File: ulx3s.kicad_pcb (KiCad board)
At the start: 4 copper layers, 60.1 x 34.8 mm, 87 parts, among them J3 hub75-abcd, J4 CONN_02X03, J5 hub75-abcd, J6 WIFI_OFF, U1 LFE5U-85F-6BG381C, U10 IS25LP128F-JBLE, U11 MPM54304GMN-0001, U2 IS42S16160J-6BL, U6 FT231XS, U9 ESP32-S3-WROOM-1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

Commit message: reassign j1 signals
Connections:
- J3 pad 1: unconnected-(J3-R1-Pad1) -> GP0
- J3 pad 10: unconnected-(J3-ROW1-Pad10) -> GN3
- J3 pad 11: unconnected-(J3-ROW2-Pad11) -> GP4
- J3 pad 12: unconnected-(J3-ROW3-Pad12) -> GN4
- J3 pad 13: unconnected-(J3-PXC-Pad13) -> GP5
- J3 pad 14: unconnected-(J3-RWL-Pad14) -> GN5
- J3 pad 15: unconnected-(J3-nOE-Pad15) -> GP6
- J3 pad 16: unconnected-(J3-GND-Pad16) -> GND
- J3 pad 2: unconnected-(J3-G1-Pad2) -> GN0
- J3 pad 3: unconnected-(J3-B1-Pad3) -> GP1
- J3 pad 4: unconnected-(J3-GND-Pad4) -> GND
- J3 pad 5: unconnected-(J3-R2-Pad5) -> GN1
- J3 pad 6: unconnected-(J3-G2-Pad6) -> GP2
- J3 pad 7: unconnected-(J3-B2-Pad7) -> GN2
- J3 pad 8: unconnected-(J3-GND-Pad8) -> GND
- J3 pad 9: unconnected-(J3-ROW0-Pad9) -> GP3
- J5 pad 1: unconnected-(J5-R1-Pad1) -> GP7
- J5 pad 10: unconnected-(J5-ROW1-Pad10) -> GN10
- J5 pad 11: unconnected-(J5-ROW2-Pad11) -> GP11
- J5 pad 12: unconnected-(J5-ROW3-Pad12) -> GN11
- J5 pad 13: unconnected-(J5-PXC-Pad13) -> GP12
- J5 pad 14: unconnected-(J5-RWL-Pad14) -> GN12
- J5 pad 15: unconnected-(J5-nOE-Pad15) -> GP13
- J5 pad 16: unconnected-(J5-GND-Pad16) -> GND
- J5 pad 2: unconnected-(J5-G1-Pad2) -> GN7
- J5 pad 3: unconnected-(J5-B1-Pad3) -> GP8
- J5 pad 4: unconnected-(J5-GND-Pad4) -> GND
- J5 pad 5: unconnected-(J5-R2-Pad5) -> GN8
- J5 pad 6: unconnected-(J5-G2-Pad6) -> GP9
- J5 pad 7: unconnected-(J5-B2-Pad7) -> GN9
- J5 pad 8: unconnected-(J5-GND-Pad8) -> GND
- J5 pad 9: unconnected-(J5-ROW0-Pad9) -> GP10
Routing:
- net unconnected-(J5-GND-Pad8): track 6.40 -> 0.00 mm
- net GND: track 305.4 -> 311.8 mm
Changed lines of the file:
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@@
 			)
 		)
-		(property "Datasheet" ""
+		(property "Datasheet" "https://www.espressif.com/sites/default/files/documentation/esp32-s3-wroom-1_wroom-1u_datasheet_en.pdf"
 			(at 0 0 90)
 			(layer "F.Fab")
@@
 			)
 		)
-		(property "Description" ""
+		(property "Description" "2.4 GHz WiFi (802.11 b/g/n) and Bluetooth ® 5 (LE) module Built around ESP32S3 series of SoCs, Xtensa ® dualcore 32bit LX7 microprocessor Flash up to 16 MB, PSRAM up to 8 MB 36 GPIOs, rich set of peripherals Onboard PCB antenna"
 			(at 0 0 90)
 			(layer "F.Fab")
@@
 			)
 		)
+		(property "Arrow" ""
+			(at 0 0 90)
+			(unlocked yes)
+			(layer "F.Fab")
+			(hide yes)
+			(effects
+				(font
+					(size 1 1)
+					(thickness 0.15)
+				)
+			)
+		)
+		(property "DatasheetLC" ""
+			(at 0 0 90)
+			(unlocked yes)
+			(layer "F.Fab")
+			(hide yes)
+			(effects
+				(font
+					(size 1 1)
+					(thickness 0.15)
+				)
+			)
+		)
+		(property "LCS_C2" ""
+			(at 0 0 90)
+			(unlocked yes)
+			(layer "F.Fab")
+			(hide yes)
+			(effects
+				(font
+					(size 1 1)
+					(thickness 0.15)
+				)
+			)
+		)
+		(property "MP_N4" ""
+			(at 0 0 90)
+			(unlocked yes)
+			(layer "F.Fab")
+			(hide yes)
+			(effects
+				(font
+					(size 1 1)
+					(thickness 0.15)
+				)
+			)
+		)
+		(property "MP_N5" ""
+			(at 0 0 90)
+			(unlocked yes)
+			(layer "F.Fab")
+			(hide yes)
+			(effects
+				(font
+					(size 1 1)
+					(thickness 0.15)
+				)
+			)
+		)
+		(property "Vertical" ""
+			(at 0 0 90)
+			(unlocked yes)
+			(layer "F.Fab")
+			(hide yes)
+			(effects
+				(font
+					(size 1 1)
+					(thickness 0.15)
+				)
+			)
+		)
+		(property "price100_Mouser" ""
+			(at 0 0 90)
+			(unlocked yes)
+			(layer "F.Fab")
+			(hide yes)
+			(effects
+				(font
+					(size 1 1)
+					(thickness 0.15)
+				)
+			)
+		)
+		(property "price1200_Chip1stop" ""
+			(at 0 0 90)
+			(unlocked yes)
+			(layer "F.Fab")
+			(hide yes)
+			(effects
+				(font
+					(size 1 1)
+					(thickness 0.15)
+				)
+			)
+		)
+		(property "price300_LCSC" ""
+			(at 0 0 90)
+			(unlocked yes)
+			(layer "F.Fab")
+			(hide yes)
+			(effects
+				(font
+					(size 1 1)
+					(thickness 0.15)
+				)
+			)
+		)
+		(property "price300_Vertical" ""
+			(at 0 0 90)
+			(unlocked yes)
+			(layer "F.Fab")
+			(hide yes)
+			(effects
+				(font
+					(size 1 1)
+					(thickness 0.15)
+				)
+			)
+		)
+		(property "price_Arrow" ""
+			(at 0 0 90)
+			(unlocked yes)
+			(layer "F.Fab")
+			(hide yes)
+			(effects
+				(font
+					(size 1 1)
+					(thickness 0.15)
+				)
+			)
+		)
+		(property "Digikey" "5407-ESP32-S3-WROOM-1-N16R8CT-ND"
+			(at 0 0 90)
+			(unlocked yes)
+			(layer "F.Fab")
+			(hide yes)
+			(effects
+				(font
+					(size 1 1)
+					(thickness 0.15)
+				)
+			)
+		)
+		(property "MPN" "356-ESP32S3WRM1N16R8"
+			(at 0 0 90)
+			(unlocked yes)
+			(layer "F.Fab")
+			(hide yes)
+			(effects
+				(font
+					(size 1 1)
+					(thickness 0.15)
+				)
+			)
+		)
 		(sheetname "/wifi/")
 		(sheetfile "wifi.kicad_sch")
+		(units
+			(unit
+				(name "A")
+				(pins "3" "8" "9" "32" "33" "34" "35" "28" "29" "30" "2" "41" "1" "40"
+					"37" "36" "14" "13" "27" "39" "38" "15" "4" "5" "6" "7" "12" "17" "18"
+					"19" "20" "21" "22" "10" "11" "23" "31" "26" "16" "24" "25"
+				)
+			)
+		)
 		(attr smd)
 		(duplicate_pad_numbers_are_jumpers no)
@@
 			(size 1.27 5.08)
 			(layers "B.Cu" "B.Paste")
-			(net "unconnected-(J3-R1-Pad1)")
+			(net "GP0")
 			(pinfunction "R1_1")
 			(pintype "input")
@@
 			(size 1.27 5.08)
 			(layers "B.Cu" "B.Paste")
-			(net "unconnected-(J3-G1-Pad2)")
+			(net "GN0")
 			(pinfunction "G1_2")
 			(pintype "input")
@@
 			(size 1.27 5.08)
 			(layers "B.Cu" "B.Paste")
-			(net "unconnected-(J3-B1-Pad3)")
+			(net "GP1")
 			(pinfunction "B1_3")
 			(pintype "input")
@@
 			(size 1.27 5.08)
 			(layers "B.Cu" "B.Paste")
-			(net "unconnected-(J3-GND-Pad4)")
+			(net "GND")
 			(pinfunction "GND_4")
 			(pintype "power_in")
@@
 			(size 1.27 5.08)
 			(layers "B.Cu" "B.Paste")
-			(net "unconnected-(J3-R2-Pad5)")
+			(net "GN1")
 			(pinfunction "R2_5")
 			(pintype "input")
@@
 			(size 1.27 5.08)
 			(layers "B.Cu" "B.Paste")
-			(net "unconnected-(J3-G2-Pad6)")
+			(net "GP2")
 			(pinfunction "G2_6")
 			(pintype "input")
@@
 			(size 1.27 5.08)
 			(layers "B.Cu" "B.Paste")
-			(net "unconnected-(J3-B2-Pad7)")
+			(net "GN2")
 			(pinfunction "B2_7")
 			(pintype "input")
@@
 			(size 1.27 5.08)
 			(layers "B.Cu" "B.Paste")
-			(net "unconnected-(J3-GND-Pad8)")
+			(net "GND")
 			(pinfunction "GND_8")
 			(pintype "power_in")
@@
 			(size 1.27 5.08)
 			(layers "B.Cu" "B.Paste")
-			(net "unconnected-(J3-ROW0-Pad9)")
+			(net "GP3")
 			(pinfunction "ROW0_9")
 			(pintype "input")
@@
 			(size 1.27 5.08)
 			(layers "B.Cu" "B.Paste")
-			(net "unconnected-(J3-ROW1-Pad10)")
+			(net "GN3")
 			(pinfunction "ROW1_10")
 			(pintype "input")
@@
 			(size 1.27 5.08)
 			(layers "B.Cu" "B.Paste")
-			(net "unconnected-(J3-ROW2-Pad11)")
+			(net "GP4")
 			(pinfunction "ROW2_11")
 			(pintype "input")
@@
 			(size 1.27 5.08)
 			(layers "B.Cu" "B.Paste")
-			(net "unconnected-(J3-ROW3-Pad12)")
+			(net "GN4")
 			(pinfunction "ROW3_12")
 			(pintype "input")
@@
 			(size 1.27 5.08)
 			(layers "B.Cu" "B.Paste")
-			(net "unconnected-(J3-PXC-Pad13)")
+			(net "GP5")
 			(pinfunction "PXC_13")
 			(pintype "input")
@@
 			(size 1.27 5.08)
 			(layers "B.Cu" "B.Paste")
-			(net "unconnected-(J3-RWL-Pad14)")
+			(net "GN5")
 			(pinfunction "RWL_14")
 			(pintype "input")
@@
 			(size 1.27 5.08)
 			(layers "B.Cu" "B.Paste")
-			(net "unconnected-(J3-nOE-Pad15)")
+			(net "GP6")
 			(pinfunction "nOE_15")
 			(pintype "input")
@@
 			(size 1.27 5.08)
 			(layers "B.Cu" "B.Paste")
-			(net "unconnected-(J3-GND-Pad16)")
+			(net "GND")
 			(pinfunction "GND_16")
 			(pintype "power_in")
@@
 			(size 1.27 5.08)
 			(layers "B.Cu" "B.Paste")
-			(net "unconnected-(J5-R1-Pad1)")
+			(net "GP7")
 			(pinfunction "R1_1")
 			(pintype "input")
@@
 			(size 1.27 5.08)
 			(layers "B.Cu" "B.Paste")
-			(net "unconnected-(J5-G1-Pad2)")
+			(net "GN7")
 			(pinfunction "G1_2")
 			(pintype "input")
@@
 			(size 1.27 5.08)
 			(layers "B.Cu" "B.Paste")
-			(net "unconnected-(J5-B1-Pad3)")
+			(net "GP8")
 			(pinfunction "B1_3")
 			(pintype "input")
@@
 			(size 1.27 5.08)
 			(layers "B.Cu" "B.Paste")
-			(net "unconnected-(J5-GND-Pad4)")
+			(net "GND")
 			(pinfunction "GND_4")
 			(pintype "power_in")
@@
 			(size 1.27 5.08)
 			(layers "B.Cu" "B.Paste")
-			(net "unconnected-(J5-R2-Pad5)")
+			(net "GN8")
 			(pinfunction "R2_5")
 			(pintype "input")
@@
 			(size 1.27 5.08)
 			(layers "B.Cu" "B.Paste")
-			(net "unconnected-(J5-G2-Pad6)")
+			(net "GP9")
 			(pinfunction "G2_6")
 			(pintype "input")
@@
 			(size 1.27 5.08)
 			(layers "B.Cu" "B.Paste")
-			(net "unconnected-(J5-B2-Pad7)")
+			(net "GN9")
 			(pinfunction "B2_7")
 			(pintype "input")
@@
 			(size 1.27 5.08)
 			(layers "B.Cu" "B.Paste")
-			(net "unconnected-(J5-GND-Pad8)")
+			(net "GND")
 			(pinfunction "GND_8")
 			(pintype "power_in")
@@
 			(size 1.27 5.08)
 			(layers "B.Cu" "B.Paste")
-			(net "unconnected-(J5-ROW0-Pad9)")
+			(net "GP10")
 			(pinfunction "ROW0_9")
 			(pintype "input")
@@
 			(size 1.27 5.08)
 			(layers "B.Cu" "B.Paste")
-			(net "unconnected-(J5-ROW1-Pad10)")
+			(net "GN10")
 			(pinfunction "ROW1_10")
 			(pintype "input")
@@
 			(size 1.27 5.08)
 			(layers "B.Cu" "B.Paste")
-			(net "unconnected-(J5-ROW2-Pad11)")
+			(net "GP11")
 			(pinfunction "ROW2_11")
 			(pintype "input")
@@
 			(size 1.27 5.08)
 			(layers "B.Cu" "B.Paste")
-			(net "unconnected-(J5-ROW3-Pad12)")
+			(net "GN11")
 			(pinfunction "ROW3_12")
 			(pintype "input")
@@
 			(size 1.27 5.08)
 			(layers "B.Cu" "B.Paste")
-			(net "unconnected-(J5-PXC-Pad13)")
+			(net "GP12")
 			(pinfunction "PXC_13")
 			(pintype "input")
@@
 			(size 1.27 5.08)
 			(layers "B.Cu" "B.Paste")
-			(net "unconnected-(J5-RWL-Pad14)")
+			(net "GN12")
 			(pinfunction "RWL_14")
 			(pintype "input")
@@
 			(size 1.27 5.08)
 			(layers "B.Cu" "B.Paste")
-			(net "unconnected-(J5-nOE-Pad15)")
+			(net "GP13")
 			(pinfunction "nOE_15")
 			(pintype "input")
@@
 			(size 1.27 5.08)
 			(layers "B.Cu" "B.Paste")
-			(net "unconnected-(J5-GND-Pad16)")
+			(net "GND")
 			(pinfunction "GND_16")
 			(pintype "power_in")
@@
 	)
 	(segment
+		(start 109.914021 100.390069)
+		(end 109.914021 93.990069)
+		(width 0.09)
+		(layer "B.Cu")
+		(net "GND")
+	)
+	(segment
 		(start 128.628319 81.093417)
 		(end 125.687714 81.093417)
@@
 		(net "/power/FB2V5")
 	)
-	(segment
-		(start 109.914021 100.390069)
-		(end 109.914021 93.990069)
-		(width 0.09)
-		(layer "B.Cu")
-		(net "unconnected-(J5-GND-Pad8)")
-	)
 	(zone

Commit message: in progress, placement happend -- working on wiring
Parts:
- removed J6: WIFI_OFF, Connector_PinHeader_2.54mm:PinHeader_1x02_P2.54mm_Vertical
- added RP7: 0, Resistor_SMD:R_0805_2012Metric_Pad1.20x1.40mm_HandSolder, F.Cu at (97.3, 94.8)
- C21, C53, R11, R12, R27, R28, R29, R30, R36, R37, R38, R39, R49, R50, R56, R62, R9: moved to F.Cu
- C48: moved to B.Cu
- J4: footprint Socket_Strips:Socket_Strip_Straight_2x03 -> Connector_PinSocket_2.54mm:PinSocket_2x03_P2.54mm_Vertical
- moved C49 67.8 mm to (174.1, 124.0)
- moved B0 62.9 mm to (109.7, 93.8), turned to 0 degrees
- moved C35 56.3 mm to (155.5, 72.8)
- moved R56 48.4 mm to (116.1, 72.2), turned to 180 degrees
- moved D28 44.4 mm to (133.5, 93.0), turned to 90 degrees
- moved D29 44.3 mm to (131.5, 93.0), turned to 90 degrees
- moved C48 44.1 mm to (177.3, 124.6)
- moved R31 43.4 mm to (129.7, 93.2)
- moved R39 43.2 mm to (97.5, 97.0), turned to 0 degrees
- moved C60 41.7 mm to (135.3, 92.6), turned to 90 degrees
- moved J4 41.6 mm to (134.8, 99.3), turned to -90 degrees
- moved R38 41.5 mm to (97.5, 98.6), turned to 180 degrees
- moved C21 41.5 mm to (97.5, 92.8)
- moved RP6 40.6 mm to (139.1, 96.2), turned to 90 degrees
- moved RB5 39.1 mm to (139.8, 92.3), turned to 180 degrees
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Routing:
- net +5V: track 41.5 -> 60.0 mm, vias 8 -> 9
- net SD_D2: track 6.48 -> 23.9 mm, vias 0 -> 1
- net GN2: track 10.3 -> 27.2 mm, vias 1 -> 0
- net GN7: track 8.16 -> 24.3 mm
- net /flash/FLASH_nCS: track 12.2 -> 27.3 mm
- net GND: track 311.8 -> 297.6 mm, vias 109 -> 107
- net /flash/FLASH_MISO: track 10.4 -> 23.4 mm
- net WIFI_USB_D-: track 5.12 -> 16.6 mm
- net /flash/FLASH_SCK: track 11.3 -> 22.2 mm
- net /flash/FLASH_nWP: track 7.60 -> 18.3 mm
- net GP1: track 12.6 -> 2.00 mm, vias 1 -> 0
- net GN1: track 13.1 -> 2.57 mm, vias 1 -> 0
- net SD_CLK: track 0.57 -> 10.8 mm, vias 1 -> 2
- net WIFI_GPIO39: track 18.4 -> 9.45 mm
- net GN4: track 9.89 -> 1.37 mm, vias 1 -> 0
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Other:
- board size 60.1 x 34.8 mm -> 60.1 x 32 mm
- copper layers 4 -> 6
- board text removed: "+1.1V"
- board text removed: "+2.5V"
- board text removed: "+3.3V"
- board text removed: "FLASH"
- board text removed: "RS232"

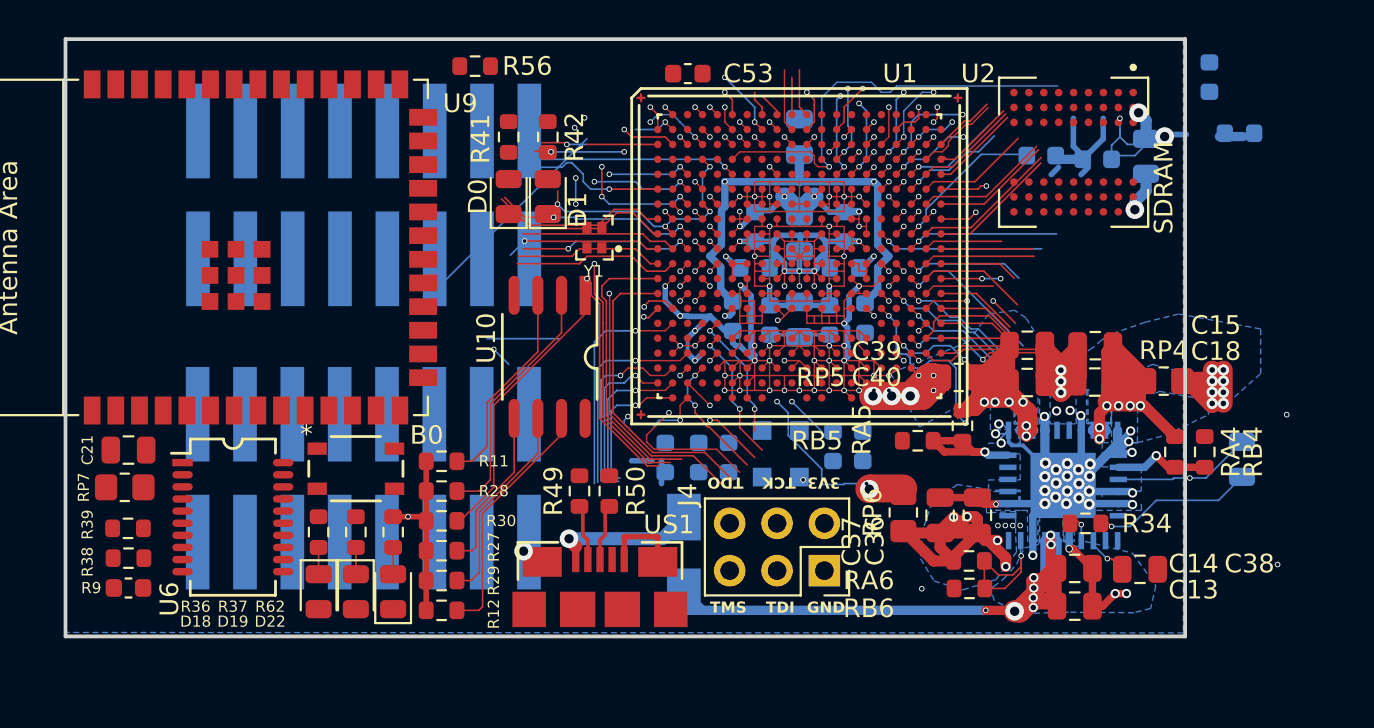
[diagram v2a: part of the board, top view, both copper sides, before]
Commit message: attempting to route memory, moved to 8layer
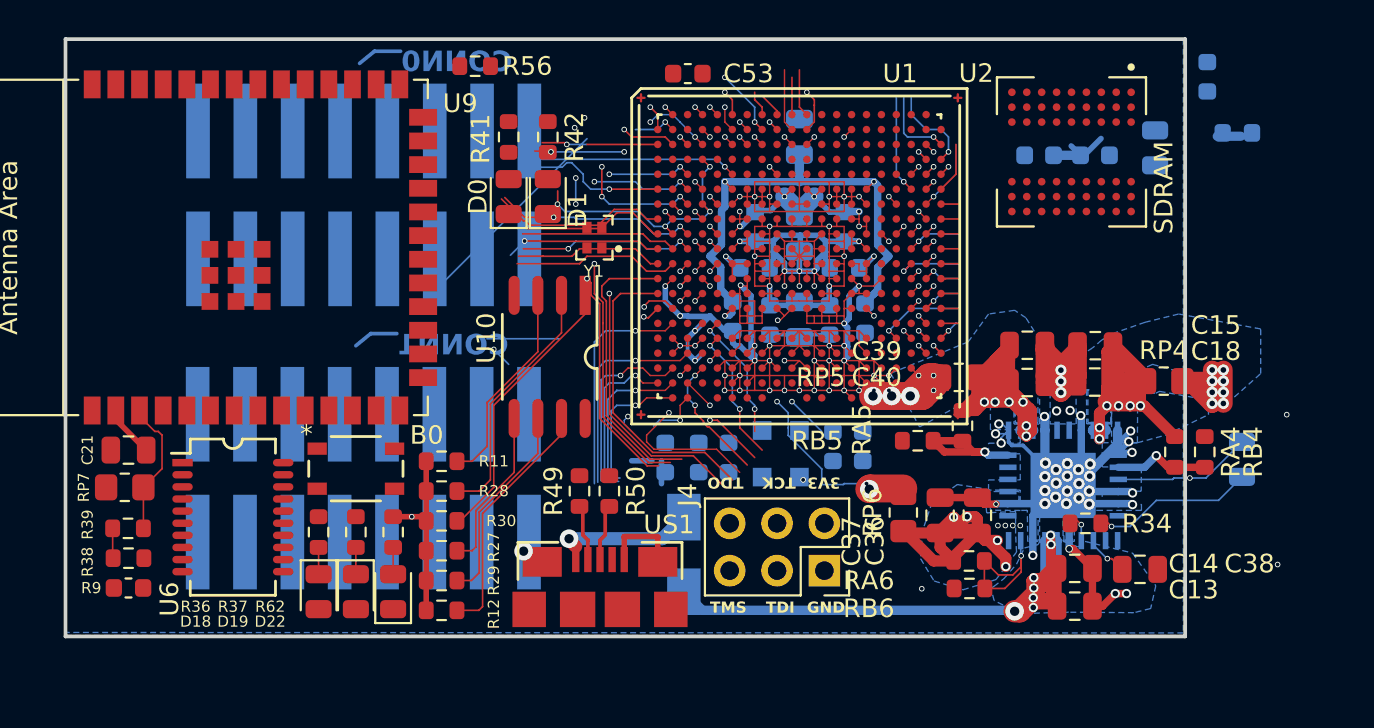
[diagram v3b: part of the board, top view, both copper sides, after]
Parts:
- moved C16 0.67 mm to (152.6, 76.6)
- moved C34 0.25 mm to (149.3, 77.0)
- moved C52 0.12 mm to (157.0, 75.8)
- moved C33 0.12 mm to (146.3, 77.0)
- moved C35 0.12 mm to (155.4, 72.8)
- moved U2 0.12 mm to (148.1, 76.8)
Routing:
- net BTN_PWRn: track 23.2 -> 0.00 mm, vias 2 -> 1
- net GN16: track 10.9 -> 0.00 mm, vias 1 -> 0
- net GN15: track 9.81 -> 0.00 mm, vias 2 -> 0
- net GND: track 297.6 -> 288.6 mm, vias 107 -> 104
- net GN22: track 8.15 -> 0.00 mm, vias 3 -> 0
- net GN27: track 7.66 -> 0.00 mm, vias 2 -> 0
- net GP15: track 7.47 -> 0.00 mm, vias 1 -> 0
- net /wifi/WIFIEN: track 0.00 -> 7.35 mm
- net GN23: track 7.17 -> 0.00 mm, vias 2 -> 0
- net GP22: track 7.07 -> 0.00 mm, vias 1 -> 0
- net GN25: track 6.83 -> 0.00 mm, vias 2 -> 0
- net GN26: track 6.62 -> 0.00 mm, vias 1 -> 0
- net GP27: track 6.54 -> 0.00 mm, vias 2 -> 0
- net GP23: track 6.07 -> 0.00 mm, vias 1 -> 0
- net SDRAM_A7: track 6.93 -> 1.00 mm
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- added copper zone on In4.Cu, net +1V1
- added copper zone on In4.Cu, net +2V5
- added copper zone on In4.Cu, net +3V3
- removed copper zone on In1.Cu, net +1V1
- removed copper zone on In1.Cu, net +2V5
- removed copper zone on In1.Cu, net +3V3
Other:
- copper layers 6 -> 8
- board text added: "CONN0"
- board text added: "CONN1"

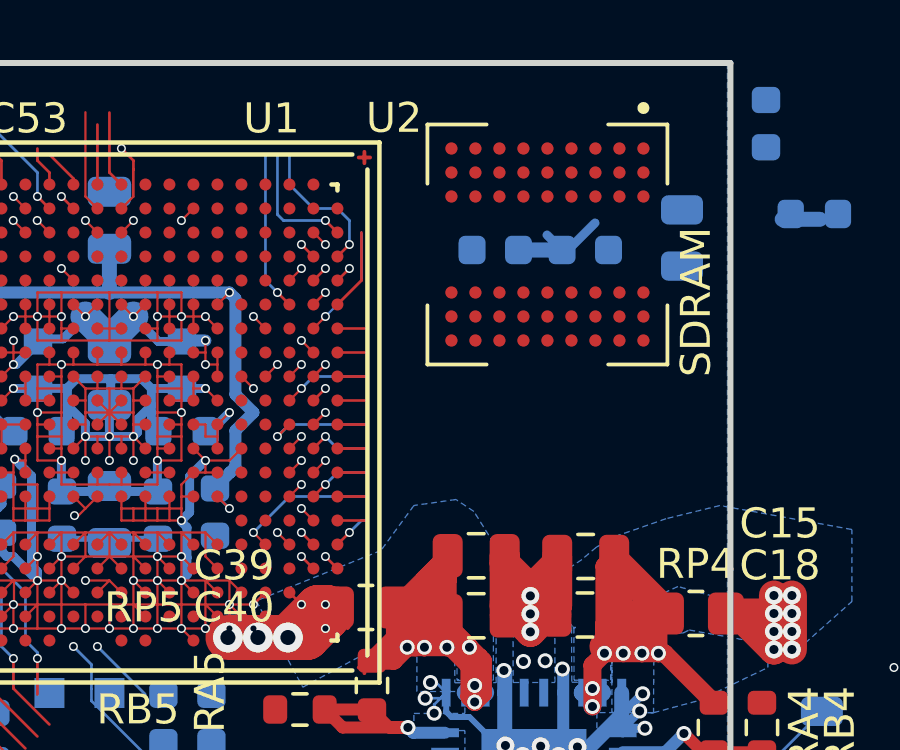
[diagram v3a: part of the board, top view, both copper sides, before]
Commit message: memory is wired
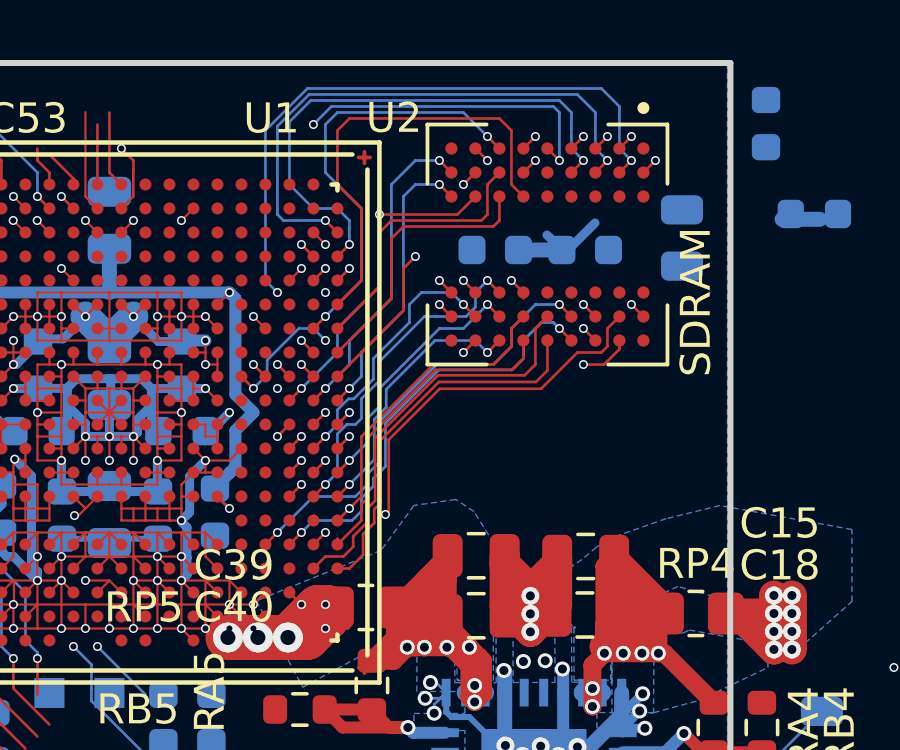
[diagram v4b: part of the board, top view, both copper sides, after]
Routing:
- net SDRAM_D15: track 7.73 -> 24.7 mm, vias 1 -> 2
- net SDRAM_D2: track 2.93 -> 18.4 mm, vias 1 -> 2
- net SDRAM_D13: track 5.33 -> 20.7 mm, vias 1 -> 2
- net SDRAM_D14: track 7.90 -> 22.6 mm, vias 1 -> 2
- net SDRAM_D11: track 4.25 -> 18.8 mm, vias 1 -> 2
- net SDRAM_A8: track 2.13 -> 16.5 mm, vias 1 -> 2
- net SDRAM_D9: track 4.86 -> 18.1 mm, vias 1 -> 2
- net SDRAM_D12: track 4.53 -> 17.8 mm, vias 1 -> 2
- net SDRAM_nCAS: track 3.26 -> 16.5 mm, vias 1 -> 3
- net SDRAM_CKE: track 2.73 -> 15.0 mm
- net SDRAM_D0: track 4.86 -> 17.0 mm, vias 1 -> 3
- net SDRAM_D10: track 3.57 -> 15.4 mm, vias 1 -> 2
- net SDRAM_D1: track 3.73 -> 15.4 mm, vias 1 -> 2
- net SDRAM_D8: track 4.53 -> 16.2 mm, vias 1 -> 3
- net SDRAM_A12: track 3.86 -> 14.4 mm, vias 1 -> 2
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
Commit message: routed conn1
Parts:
- moved C53 2.61 mm to (127.7, 70.0)
- moved R56 1.40 mm to (116.1, 73.6)
- moved R49 0.60 mm to (121.7, 95.6)
- moved R50 0.60 mm to (123.3, 95.6)
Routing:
- net USB_FTDI_D-: track 19.0 -> 52.8 mm, vias 0 -> 2
- net USB_FTDI_D+: track 19.1 -> 52.8 mm, vias 0 -> 2
- net GP1: track 2.00 -> 35.3 mm, vias 0 -> 1
- net GN1: track 2.57 -> 32.5 mm, vias 0 -> 4
- net GN4: track 1.37 -> 29.1 mm, vias 0 -> 2
- net GN5: track 3.63 -> 29.7 mm
- net GP4: track 0.00 -> 23.4 mm, vias 0 -> 1
- net GN0: track 23.8 -> 44.3 mm, vias 1 -> 2
- net GP2: track 14.8 -> 35.1 mm, vias 0 -> 2
- net GN3: track 12.1 -> 31.4 mm, vias 1 -> 2
- net GN7: track 24.3 -> 5.97 mm
- net GP0: track 22.4 -> 39.2 mm
- net GP5: track 4.52 -> 21.0 mm, vias 1 -> 3
- net GP3: track 10.7 -> 26.6 mm
- net WIFI_EN: track 20.5 -> 6.47 mm
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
